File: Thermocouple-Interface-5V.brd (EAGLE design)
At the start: 38.1 x 31.8 mm, 17 parts, among them U1 MAX31855, U3 LP298XS

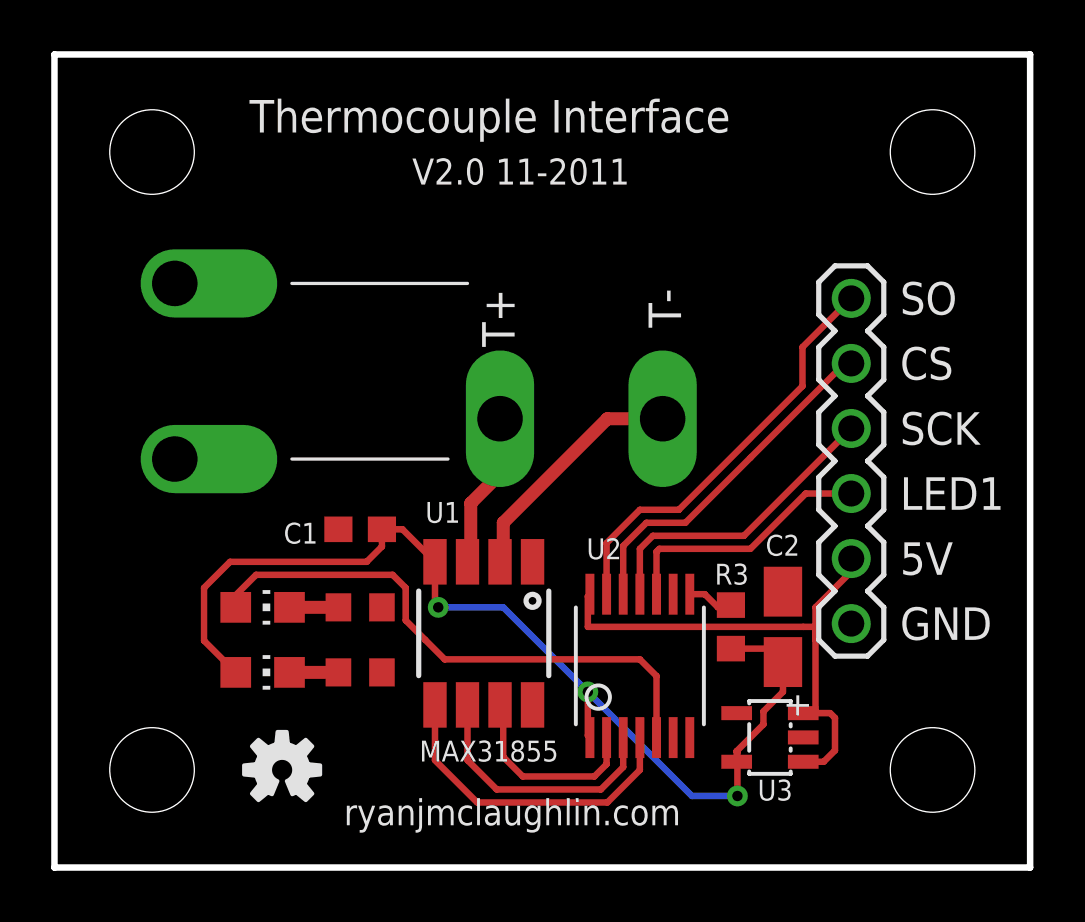
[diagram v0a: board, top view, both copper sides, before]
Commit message: Status led no longer routes through level shifter, bumped to v2.0.1 for 01-2012 pcb production
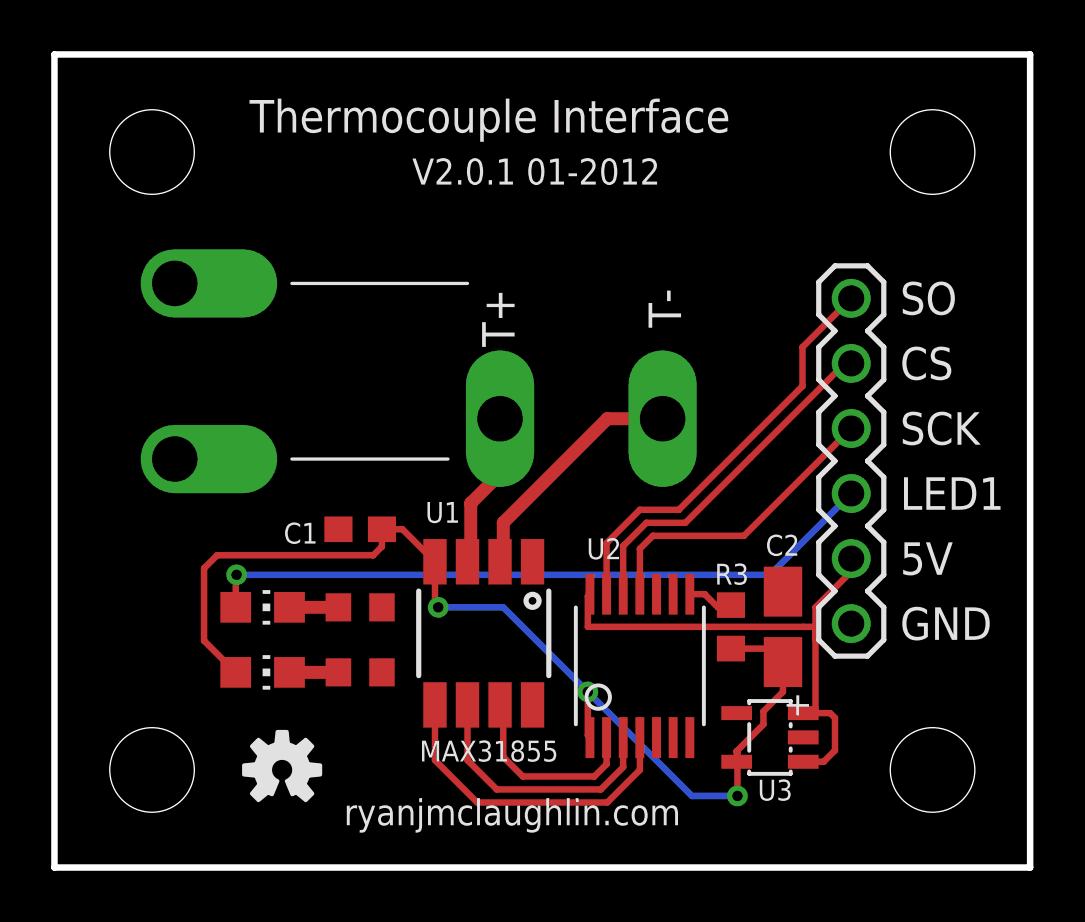
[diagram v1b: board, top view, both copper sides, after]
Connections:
- removed net STATUS: D1.A, U2.5
- removed net _STATUS: JP1.4, U2.10
- new net N$4: D1.A, JP1.4
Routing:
- net N$4: track 0.00 -> 26.6 mm, vias 0 -> 1
- net STATUS: track 22.0 -> 0.00 mm
- net _STATUS: track 10.2 -> 0.00 mm
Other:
- board text added: "V2.0.1 01-2012"
- board text removed: "V2.0 11-2011"
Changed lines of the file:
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@@
 <text x="7.62" y="28.702" size="1.27" layer="21">Thermocouple Interface</text>
 <text x="11.303" y="1.651" size="1.016" layer="21" font="vector">ryanjmclaughlin.com</text>
-<text x="13.97" y="26.67" size="1.016" layer="21">V2.0 11-2011</text>
+<text x="13.97" y="26.67" size="1.016" layer="21">V2.0.1 01-2012</text>
 <text x="33.02" y="21.59" size="1.27" layer="21">SO</text>
 <text x="33.02" y="19.05" size="1.27" layer="21">CS</text>
@@
 <wire x1="24.892" y1="2.794" x2="26.67" y2="2.794" width="0.254" layer="16"/>
 <wire x1="7.078" y1="7.62" x2="5.842" y2="8.856" width="0.254" layer="1"/>
-<wire x1="5.842" y1="8.856" x2="5.842" y2="10.922" width="0.254" layer="1"/>
-<wire x1="5.842" y1="10.922" x2="6.858" y2="11.938" width="0.254" layer="1"/>
-<wire x1="6.858" y1="11.938" x2="12.192" y2="11.938" width="0.254" layer="1"/>
-<wire x1="12.192" y1="11.938" x2="12.788" y2="12.534" width="0.254" layer="1"/>
+<wire x1="5.842" y1="8.856" x2="5.842" y2="11.684" width="0.254" layer="1"/>
 <wire x1="12.788" y1="12.534" x2="12.788" y2="13.208" width="0.254" layer="1"/>
 <wire x1="13.589" y1="13.208" x2="14.859" y2="11.938" width="0.254" layer="1"/>
@@
 <via x="14.986" y="10.16" extent="1-16" drill="0.4064" diameter="0.8128"/>
 <via x="26.67" y="2.794" extent="1-16" drill="0.4064" diameter="0.8128"/>
+<wire x1="12.788" y1="12.534" x2="12.446" y2="12.192" width="0.254" layer="1"/>
+<wire x1="12.446" y1="12.192" x2="6.35" y2="12.192" width="0.254" layer="1"/>
+<wire x1="6.35" y1="12.192" x2="5.842" y2="11.684" width="0.254" layer="1"/>
 </signal>
 <signal name="SO">
@@
 <wire x1="22.86" y1="3.81" x2="22.86" y2="5.074" width="0.254" layer="1"/>
 </signal>
-<signal name="STATUS">
-<contactref element="U2" pad="5"/>
-<contactref element="D1" pad="A"/>
-<wire x1="14.478" y1="8.89" x2="15.24" y2="8.128" width="0.254" layer="1"/>
-<wire x1="23.51" y1="7.478" x2="23.51" y2="5.074" width="0.254" layer="1"/>
-<wire x1="22.86" y1="8.128" x2="23.51" y2="7.478" width="0.254" layer="1"/>
-<wire x1="15.24" y1="8.128" x2="22.86" y2="8.128" width="0.254" layer="1"/>
-<wire x1="13.716" y1="9.652" x2="14.478" y2="8.89" width="0.254" layer="1"/>
-<wire x1="13.716" y1="10.922" x2="13.716" y2="9.652" width="0.254" layer="1"/>
-<wire x1="13.208" y1="11.43" x2="13.716" y2="10.922" width="0.254" layer="1"/>
-<wire x1="7.874" y1="11.43" x2="13.208" y2="11.43" width="0.254" layer="1"/>
-<wire x1="7.078" y1="10.634" x2="7.874" y2="11.43" width="0.254" layer="1"/>
-<wire x1="7.078" y1="10.16" x2="7.078" y2="10.634" width="0.254" layer="1"/>
-</signal>
 <signal name="_SO">
 <contactref element="U2" pad="13"/>
@@
 <wire x1="26.924" y1="12.954" x2="31.115" y2="17.145" width="0.254" layer="1"/>
 </signal>
-<signal name="_STATUS">
-<contactref element="U2" pad="10"/>
-<contactref element="JP1" pad="4"/>
-<wire x1="23.51" y1="10.674" x2="23.51" y2="12.334" width="0.254" layer="1"/>
-<wire x1="23.51" y1="12.334" x2="23.622" y2="12.446" width="0.254" layer="1"/>
-<wire x1="29.337" y1="14.605" x2="31.115" y2="14.605" width="0.254" layer="1"/>
-<wire x1="27.178" y1="12.446" x2="29.337" y2="14.605" width="0.254" layer="1"/>
-<wire x1="23.622" y1="12.446" x2="27.178" y2="12.446" width="0.254" layer="1"/>
-</signal>
 <signal name="N$3">
 <contactref element="U2" pad="8"/>
@@
 <wire x1="26.328" y1="10.16" x2="26.416" y2="10.248" width="0.254" layer="1"/>
 </signal>
+<signal name="N$4">
+<contactref element="JP1" pad="4"/>
+<contactref element="D1" pad="A"/>
+<wire x1="31.115" y1="14.605" x2="27.94" y2="11.43" width="0.254" layer="16"/>
+<wire x1="27.94" y1="11.43" x2="7.112" y2="11.43" width="0.254" layer="16"/>
+<via x="7.112" y="11.43" extent="1-16" drill="0.4064" diameter="0.8128"/>
+<wire x1="7.112" y1="11.43" x2="7.078" y2="11.396" width="0.254" layer="1"/>
+<wire x1="7.078" y1="11.396" x2="7.078" y2="10.16" width="0.254" layer="1"/>
+</signal>
 </signals>
